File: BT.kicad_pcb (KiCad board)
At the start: 4 copper layers, 55 x 40 mm, 95 parts, among them J1 61300511121, J2 Conn_01x03_Pin, J3 S6B-PH-K-S, J4 Boxed_Header_02x03_SMT, K1 AGQ200A12Z, Q1 BSS123, U1 PCM5100A, U2 ESP32-WROOM-32U, U3 TLV4888DR, U4 TLVM23615RDNR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

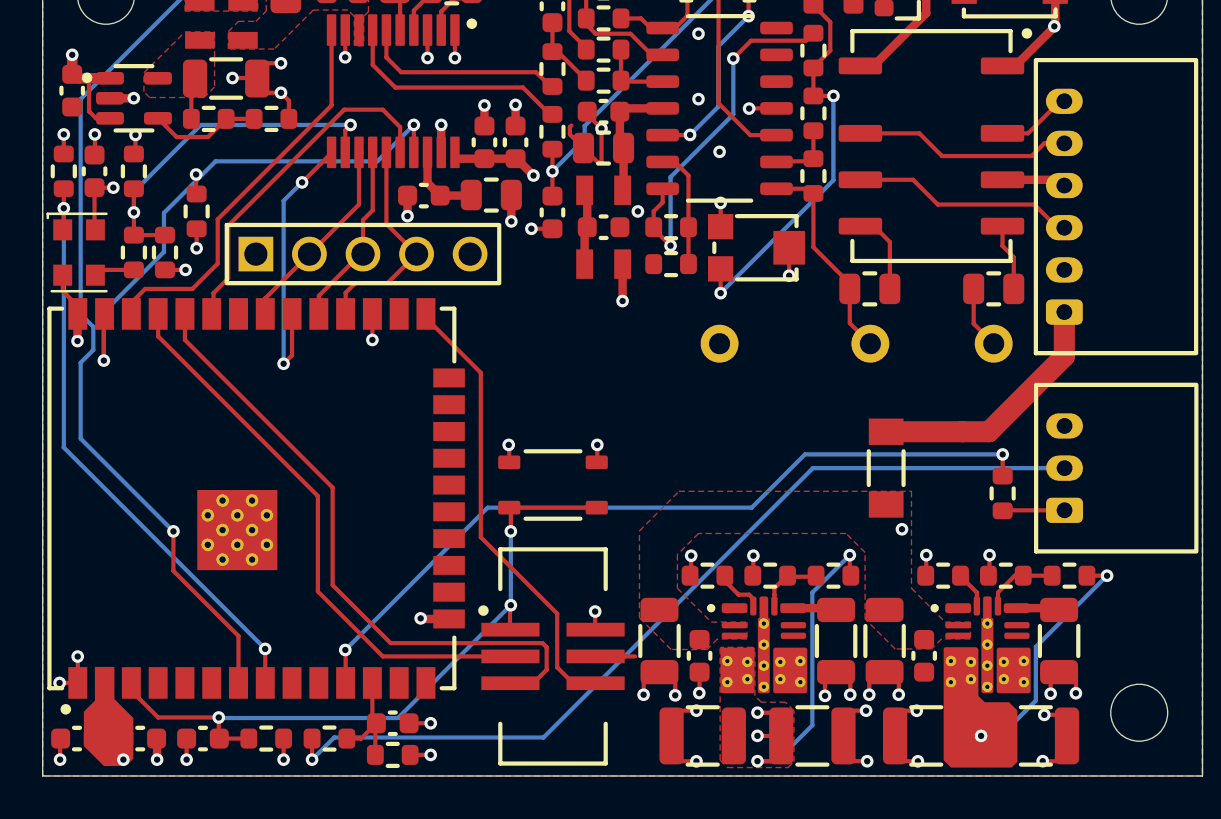
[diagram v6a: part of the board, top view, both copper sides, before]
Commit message: added teardrops
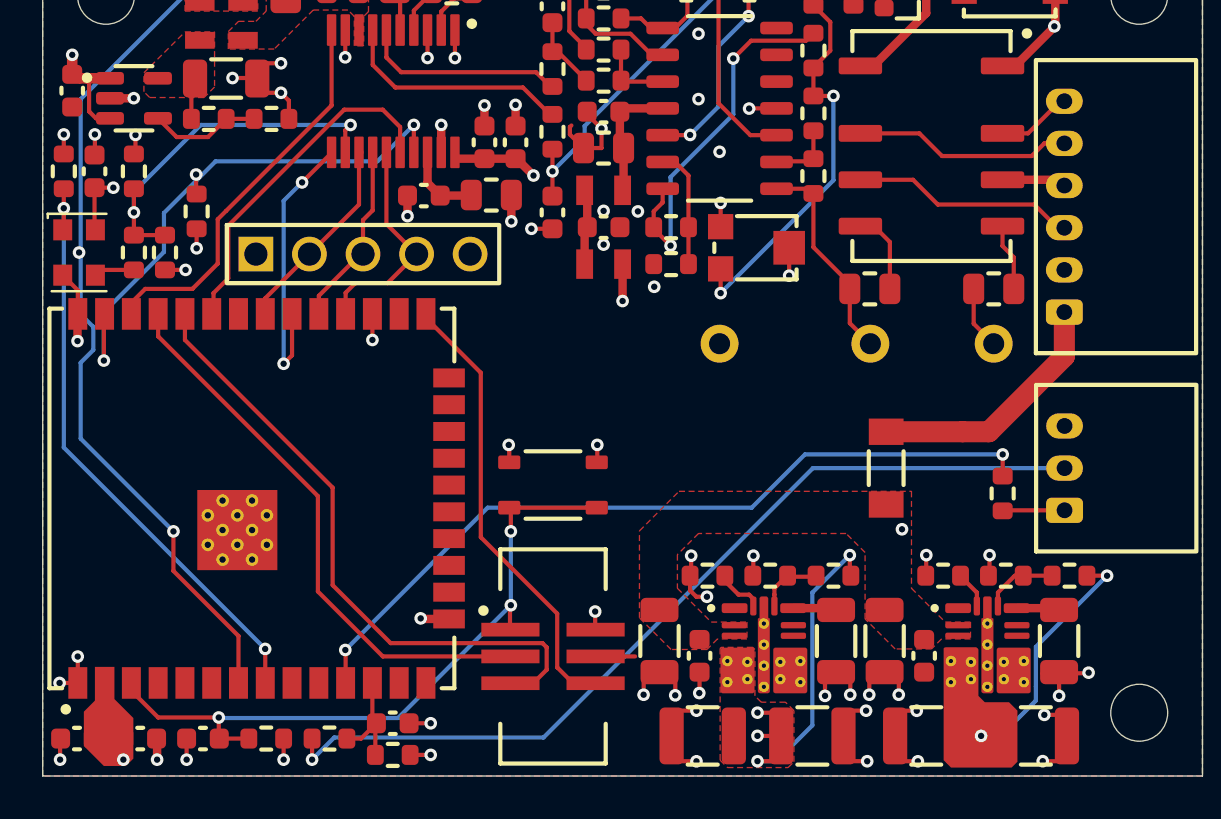
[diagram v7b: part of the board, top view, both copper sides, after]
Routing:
- net GND: track 73.0 -> 73.2 mm, vias 58 -> 62
- net /SW_TO_BT_AUDIO: vias 2 -> 3

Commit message: added signals
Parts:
- removed C22: 100nF, NRD_CAP:C_0603
- removed R35, R6: 1K, NRD_RES:R_0603
- removed R7: 10K, NRD_RES:R_0603
- added C28: 100nF, NRD_CAP:C_0603, F.Cu at (165.2, 102.9)
- added C34: 100nF, NRD_CAP:C_0603, F.Cu at (165.2, 101.3)
- added Q2: BSS123, NRD_MOSFET:BSS123, F.Cu at (152.2, 99.7)
- added R38: 10K, NRD_RES:R_0603, F.Cu at (162.2, 102.9)
- added R39: 10K, NRD_RES:R_0603, F.Cu at (162.2, 101.3)
- added R40: 1K, NRD_RES:R_0603, F.Cu at (165.2, 99.7)
- J2: value Conn_01x03_Pin -> S6B-PH-K-S; footprint NRD_CON:S3B-PH-K-S -> NRD_CON:S6B-PH-K-S
- M1, M2, M3: value (none) -> Mounting_Hole_2.7mm_Unplated
- S1: value Untitled -> 434123025826
- moved R34 28.7 mm to (154.6, 99.7)
- moved J4 10.3 mm to (145.0, 99.8)
- moved S1 9.87 mm to (143.7, 111.7), turned to -90 degrees
- moved R17 5.74 mm to (163.9, 104.5), turned to 0 degrees
- moved C18 2.46 mm to (160.0, 109.8)
- moved C19 2.46 mm to (158.2, 109.1)
- moved C20 2.46 mm to (149.4, 109.8)
- moved C24 2.46 mm to (149.5, 113.6)
- moved C30 2.46 mm to (160.1, 113.6)
- moved R18 2.46 mm to (149.8, 106.0)
- moved R20 2.46 mm to (163.9, 106.0)
- moved U5 2.46 mm to (163.0, 109.5)
- moved C17 2.46 mm to (147.5, 109.1)
- moved C23 2.46 mm to (155.9, 109.1)
- moved C25 2.46 mm to (154.7, 113.6)
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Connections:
- J2 pad 1: /LED_CON -> GND
- J2 pad 2: /BUTTON_CON -> /~{BT_EN}
- J2 pad 3: GND -> /FWD_CON
- Q1 pad 1: /SW_TO_BT_AUDIO -> /BT_EN
- R34 pad 1: /DAC_MUTEn -> +3V3
- R34 pad 2: GND -> /~{BT_EN}
- R8 pad 1: /SW_TO_BT_AUDIO -> /BT_EN
- U2 pad 11: /LED -> /DAC_MCLK_EN
- U2 pad 12: /Button -> /FWD_CON
- U2 pad 6: unconnected-(U2-IO34-Pad6) -> /BT_EN
- U2 pad 7: /SW_TO_BT_AUDIO -> unconnected-(U2-IO35-Pad7)
- U2 pad 8: /DAC_MCLK_EN -> /REV_CON
- U2 pad 9: unconnected-(U2-IO33-Pad9) -> /LED
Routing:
- net /BT_EN: track 0.00 -> 127.1 mm, vias 0 -> 3
- net /SW_TO_BT_AUDIO: track 77.0 -> 0.00 mm, vias 3 -> 0
- net /REV_CON: track 0.00 -> 47.5 mm, vias 0 -> 2
- net /BUTTON_CON: track 42.4 -> 0.00 mm, vias 1 -> 0
- net /FWD_CON: track 0.00 -> 40.8 mm, vias 0 -> 2
- net /~{BT_EN}: track 0.00 -> 20.1 mm
- net /ESP_TXD0: track 26.7 -> 38.5 mm
- net /KL30: track 12.0 -> 19.1 mm, vias 0 -> 3
- net /ESP_EN: track 33.7 -> 40.4 mm, vias 3 -> 0
- net /DAC_MCLK_EN: track 28.4 -> 33.8 mm
- net /Button: track 5.21 -> 0.00 mm
- net GND: track 73.2 -> 68.1 mm, vias 62 -> 60
- net +12V: track 34.5 -> 37.7 mm
- net /DAC_MUTEn: track 26.3 -> 23.3 mm, vias 3 -> 2
- net /ESP_IO0: track 21.5 -> 18.9 mm
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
